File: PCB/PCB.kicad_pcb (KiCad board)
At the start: 2 copper layers, 50 parts, among them J2 Conn_01x02_Pin, J3 Conn_01x02_Pin, J5 Conn_01x04_Pin, SW1 SW_Push, U1 STM32L476RGTx, U2 FGPMMOPA6H, U4 TPS63001DRCR, U5 LM2735XMF/NOPB, U8 LM386, U9 MAX7375AXR805

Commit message: Add files via upload
Finished PCB, awaiting check from professor and TAs
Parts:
- added H1: MountingHole, MountingHole:MountingHole_2.1mm, F.Cu at (232.4, 141.0)
- added H2: MountingHole, MountingHole:MountingHole_2.1mm, F.Cu at (209.6, 88.9)
- added H3: MountingHole, MountingHole:MountingHole_2.1mm, F.Cu at (184.2, 116.8)
- added H4: MountingHole, MountingHole:MountingHole_2.1mm, F.Cu at (185.4, 139.7)
- moved U3 111.5 mm to (200.7, 135.9), turned to -90 degrees
- moved C11 90.8 mm to (185.4, 124.6), turned to 90 degrees
- moved C1 90.5 mm to (206.2, 97.2)
- moved C2 90.5 mm to (206.2, 104.2)
- moved C3 90.5 mm to (178.2, 106.0)
- moved C4 90.5 mm to (183.2, 96.5)
- moved C5 90.5 mm to (192.7, 105.1)
- moved D1 90.5 mm to (196.7, 97.6)
- moved D3 90.5 mm to (193.2, 95.9)
- moved J2 90.5 mm to (199.2, 88.5)
- moved L1 90.5 mm to (210.7, 100.7)
- moved L2 90.5 mm to (181.0, 91.0)
- moved R1 90.5 mm to (183.2, 104.0)
- moved R2 90.5 mm to (187.7, 96.5)
- moved R3 90.5 mm to (183.3, 99.5)
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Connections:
- U1 pad 24: unconnected-(U1-PC4-Pad24) -> /LoRa RX
- U1 pad 25: unconnected-(U1-PC5-Pad25) -> /LoRa TX
- U1 pad 27: /Debug 4 -> unconnected-(U1-PB1-Pad27)
- U1 pad 28: /Debug 3 -> unconnected-(U1-PB2-Pad28)
- U1 pad 29: /Debug 2 -> unconnected-(U1-PB10-Pad29)
- U1 pad 30: /Debug 1 -> unconnected-(U1-PB11-Pad30)
- U1 pad 33: unconnected-(U1-PB12-Pad33) -> /Debug 4
- U1 pad 34: unconnected-(U1-PB13-Pad34) -> /Debug 2
- U1 pad 35: unconnected-(U1-PB14-Pad35) -> /Debug 3
- U1 pad 36: unconnected-(U1-PB15-Pad36) -> /Debug 1
- U1 pad 53: /LoRa RX -> unconnected-(U1-PC12-Pad53)
- U1 pad 54: /LoRa TX -> unconnected-(U1-PD2-Pad54)
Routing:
- net GND: track 105.9 -> 231.3 mm, vias 21 -> 59
- net +3.3V: track 67.0 -> 145.3 mm, vias 5 -> 9
- net /RST: track 19.1 -> 63.4 mm
- net /GPS RX: track 0.00 -> 35.3 mm, vias 0 -> 2
- net /GPS TX: track 0.00 -> 31.3 mm, vias 0 -> 2
- net +5V: track 28.2 -> 58.1 mm, vias 3 -> 5
- net /SWCLK: track 0.00 -> 28.9 mm, vias 0 -> 1
- net /SWDIO: track 0.00 -> 23.9 mm, vias 0 -> 1
- net /LoRa TX: track 0.00 -> 20.5 mm, vias 0 -> 1
- net /LoRa RX: track 0.00 -> 17.7 mm, vias 0 -> 1
- net /Debug 3: track 0.00 -> 17.3 mm
- net /DAC OUT: track 0.00 -> 16.7 mm, vias 0 -> 1
- net /Debug 2: track 0.00 -> 16.3 mm
- net /Debug 1: track 0.00 -> 15.2 mm
- net /Debug 4: track 0.00 -> 11.5 mm
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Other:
- board text added: "ECE 477 Team 5: Smart Dog Collar Andrew Wu Nick Durnil David Manojlovic Ethan James Version 2"

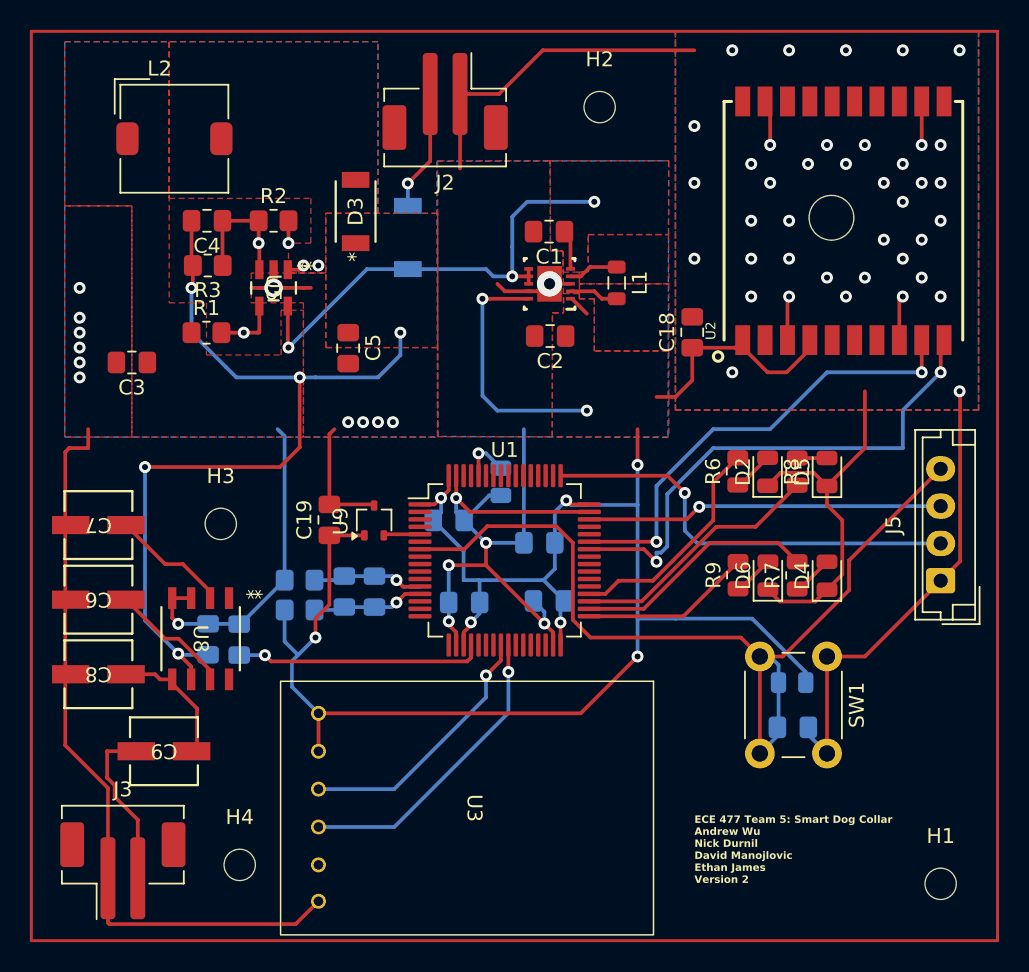
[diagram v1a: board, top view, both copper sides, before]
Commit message: Exlusion Zones added
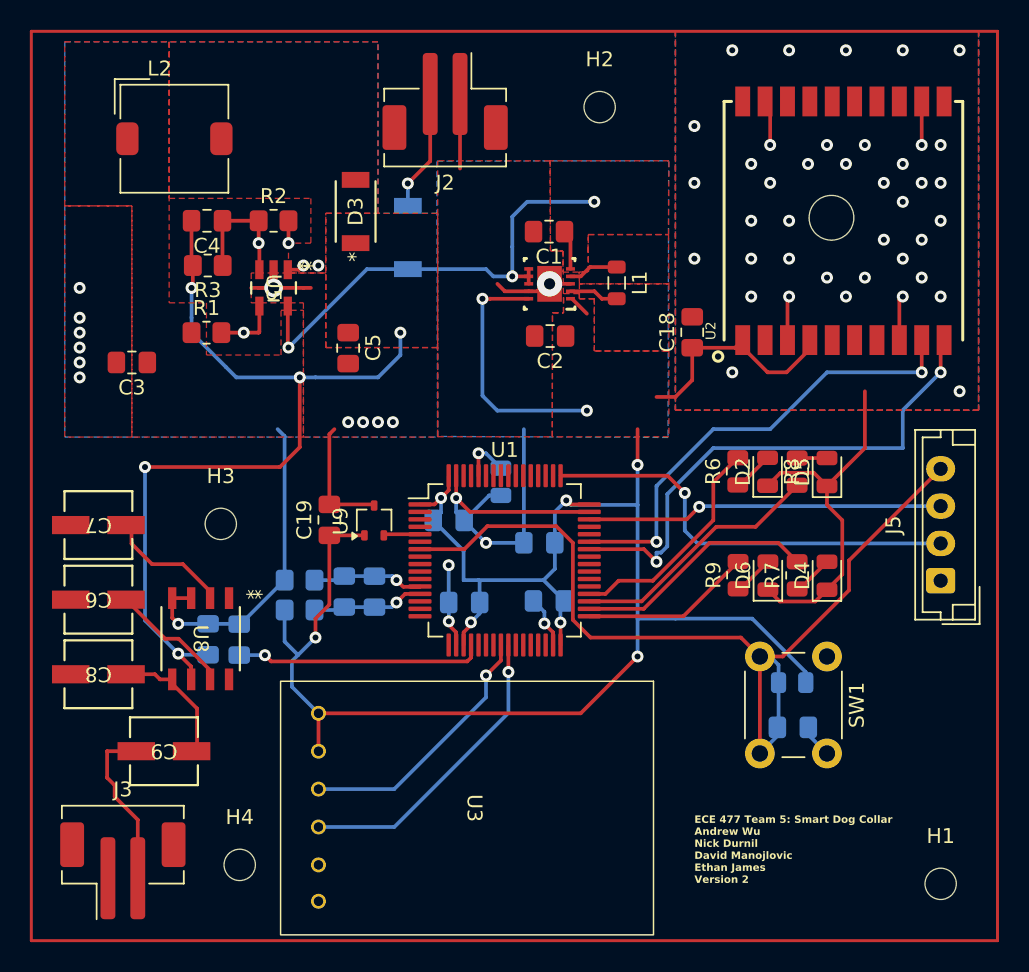
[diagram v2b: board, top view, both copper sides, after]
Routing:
- net GND: track 231.3 -> 124.1 mm
- net /- Amp: track 7.93 -> 8.44 mm

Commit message: DRC Error fixes
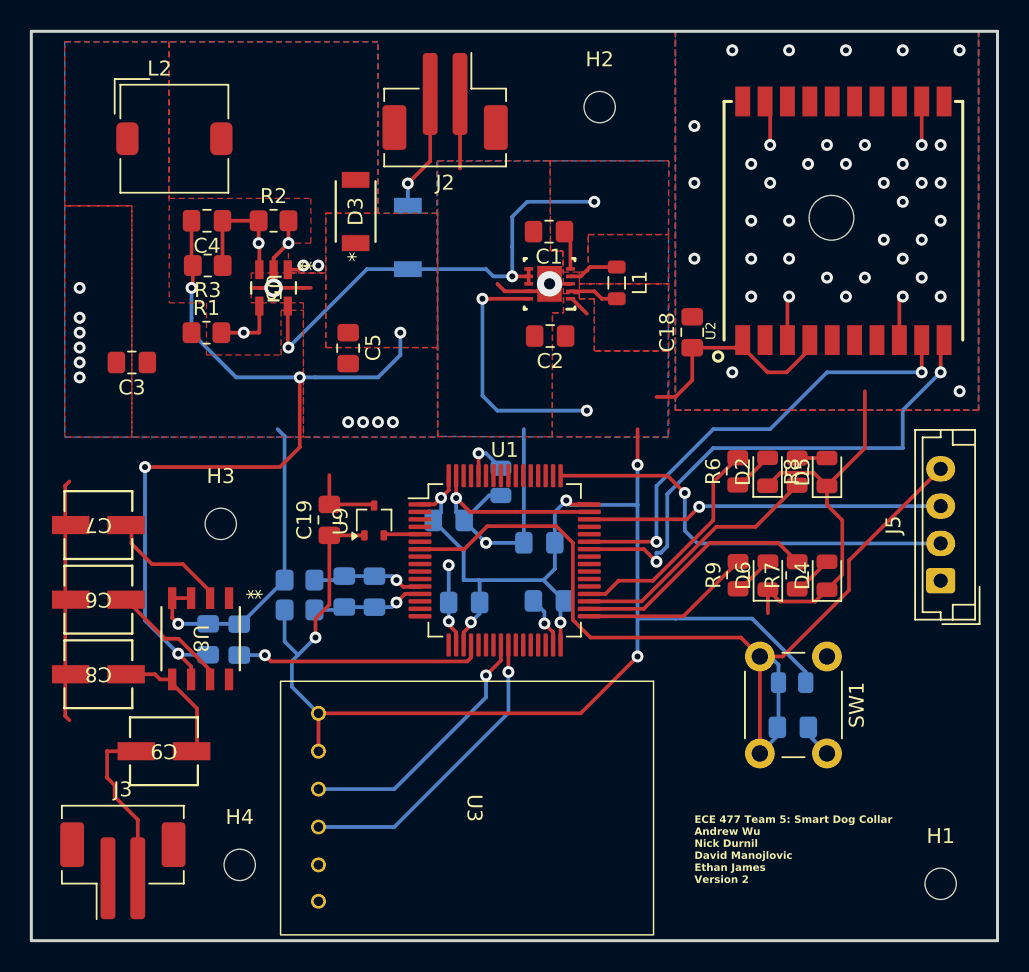
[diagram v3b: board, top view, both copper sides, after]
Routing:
- net GND: track 124.1 -> 141.8 mm
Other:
- board outline added: 64.8 x 61 mm
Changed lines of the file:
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@@
 		)
 		(fill none)
-		(layer "F.Cu")
-		(net 2)
+		(layer "Edge.Cuts")
 	)
 	(gr_text "ECE 477 Team 5: Smart Dog Collar\nAndrew Wu\nNick Durnil\nDavid Manojlovic\nEthan James\nVersion 2"
@@
 	)
 	(segment
-		(start 191.43 115.535)
-		(end 191.43 110.83)
-		(width 0.25)
-		(layer "F.Cu")
-		(net 2)
-	)
-	(segment
 		(start 222.14 104.52)
 		(end 222.14 101.71)
@@
 	)
 	(segment
+		(start 173.7253 129.7253)
+		(end 174 130)
+		(width 0.25)
+		(layer "F.Cu")
+		(net 2)
+	)
+	(segment
 		(start 220.82801 121.243481)
 		(end 221.627029 122.0425)
@@
 	)
 	(segment
+		(start 173.7253 114.2747)
+		(end 174 114)
+		(width 0.25)
+		(layer "F.Cu")
+		(net 2)
+	)
+	(segment
 		(start 205.362145 101.247732)
 		(end 204.792148 101.247732)
@@
 	)
 	(segment
-		(start 187.69 99.8008)
-		(end 187.69 101.02)
+		(start 220.82801 121.243481)
+		(end 220.82801 122.82801)
+		(width 0.25)
+		(layer "F.Cu")
+		(net 2)
+	)
+	(segment
+		(start 173.7253 116.5537)
+		(end 173.7253 114.2747)
+		(width 0.25)
+		(layer "F.Cu")
+		(net 2)
+	)
+	(segment
+		(start 174.0916 126.92)
+		(end 173.7253 127.2863)
 		(width 0.25)
 		(layer "F.Cu")
@@
 	)
 	(segment
+		(start 173.7253 127.2863)
+		(end 173.7253 129.7253)
+		(width 0.25)
+		(layer "F.Cu")
+		(net 2)
+	)
+	(segment
 		(start 182.165 121.81585)
 		(end 180.895 121.81585)
@@
 	)
 	(segment
+		(start 174.0916 116.92)
+		(end 173.7253 116.5537)
+		(width 0.25)
+		(layer "F.Cu")
+		(net 2)
+	)
+	(segment
+		(start 187.69 99.02)
+		(end 188.69 98.02)
+		(width 0.25)
+		(layer "F.Cu")
+		(net 2)
+	)
+	(segment
 		(start 186.69 101.02)
 		(end 187.69 101.02)
@@
 	)
 	(segment
+		(start 191.43 115.535)
+		(end 191.43 113.57)
+		(width 0.25)
+		(layer "F.Cu")
+		(net 2)
+	)
+	(segment
+		(start 173.7253 126.5537)
+		(end 173.7253 122.2863)
+		(width 0.25)
+		(layer "F.Cu")
+		(net 2)
+	)
+	(segment
 		(start 221.675735 113.4125)
 		(end 223.9025 113.4125)
@@
 	)
 	(segment
+		(start 187.69 99.8008)
+		(end 187.69 99.02)
+		(width 0.25)
+		(layer "F.Cu")
+		(net 2)
+	)
+	(segment
 		(start 180.895 121.81585)
 		(end 180.895 123.135)
@@
 	)
 	(segment
+		(start 174.0916 126.92)
+		(end 173.7253 126.5537)
+		(width 0.25)
+		(layer "F.Cu")
+		(net 2)
+	)
+	(segment
 		(start 220.98 89.36)
 		(end 220.98 91.44)
@@
 	)
 	(segment
+		(start 173.7253 121.5537)
+		(end 173.7253 117.2863)
+		(width 0.25)
+		(layer "F.Cu")
+		(net 2)
+	)
+	(segment
 		(start 186.69 101.02)
 		(end 186.19 101.02)
@@
 	)
 	(segment
+		(start 187.69 99.8008)
+		(end 187.69 101.02)
+		(width 0.25)
+		(layer "F.Cu")
+		(net 2)
+	)
+	(segment
 		(start 221.627029 122.0425)
 		(end 224.0025 122.0425)
@@
 	)
 	(segment
+		(start 173.7253 122.2863)
+		(end 174.0916 121.92)
+		(width 0.25)
+		(layer "F.Cu")
+		(net 2)
+	)
+	(segment
+		(start 173.7253 117.2863)
+		(end 174.0916 116.92)
+		(width 0.25)
+		(layer "F.Cu")
+		(net 2)
+	)
+	(segment
 		(start 204.792148 101.247732)
 		(end 203.19215 101.247732)
@@
 	)
 	(segment
-		(start 191.43 110.83)
-		(end 191.77 110.49)
+		(start 174.0916 121.92)
+		(end 173.7253 121.5537)
 		(width 0.25)
 		(layer "F.Cu")
@@
 		(polygon
 			(pts
-				(xy 190.5 114) (xy 190.5 119) (xy 196 119) (xy 196 114)
+				(xy 190 114) (xy 190 119) (xy 196 119) (xy 196 114)
 			)
 		)
@@
 		(net_name "")
 		(layers "F&B.Cu")
-		(name "Mounting Hole")
 		(hatch edge 0.5)
 		(connect_pads
@@
 		(polygon
 			(pts
-				(xy 181.5 114.5) (xy 181.5 119) (xy 187 119) (xy 187 114.5)
+				(xy 181.5 114) (xy 187 114) (xy 187 119) (xy 186 119) (xy 184 119.5) (xy 182.5 119) (xy 181.5 119)
 			)
 		)
@@
 		(polygon
 			(pts
-				(xy 207 86.5) (xy 207 91.5) (xy 212.5 91.5) (xy 212.5 86.5)
+				(xy 206.815912 86.399459) (xy 206.815912 91.399459) (xy 212.315912 91.399459) (xy 212.315912 86.399459)
 			)
 		)

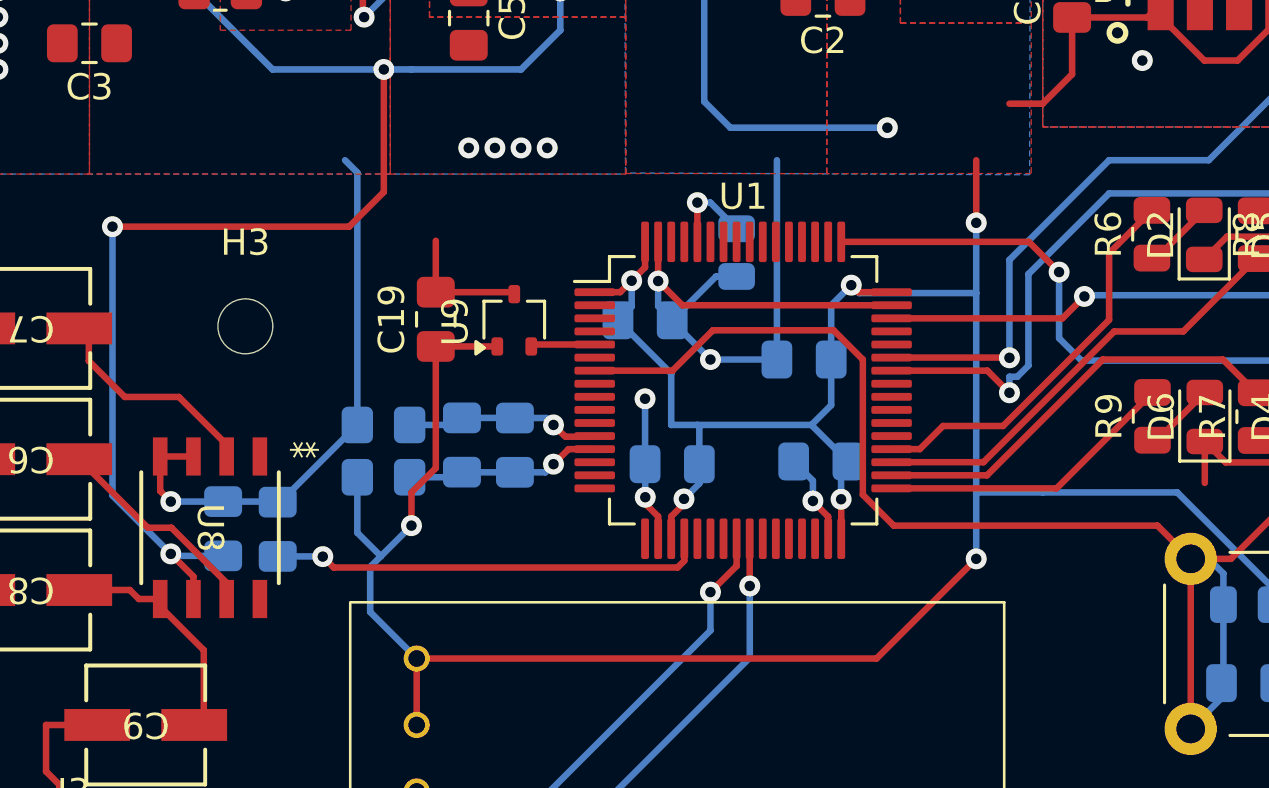
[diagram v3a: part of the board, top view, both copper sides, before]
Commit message: Debug vias added
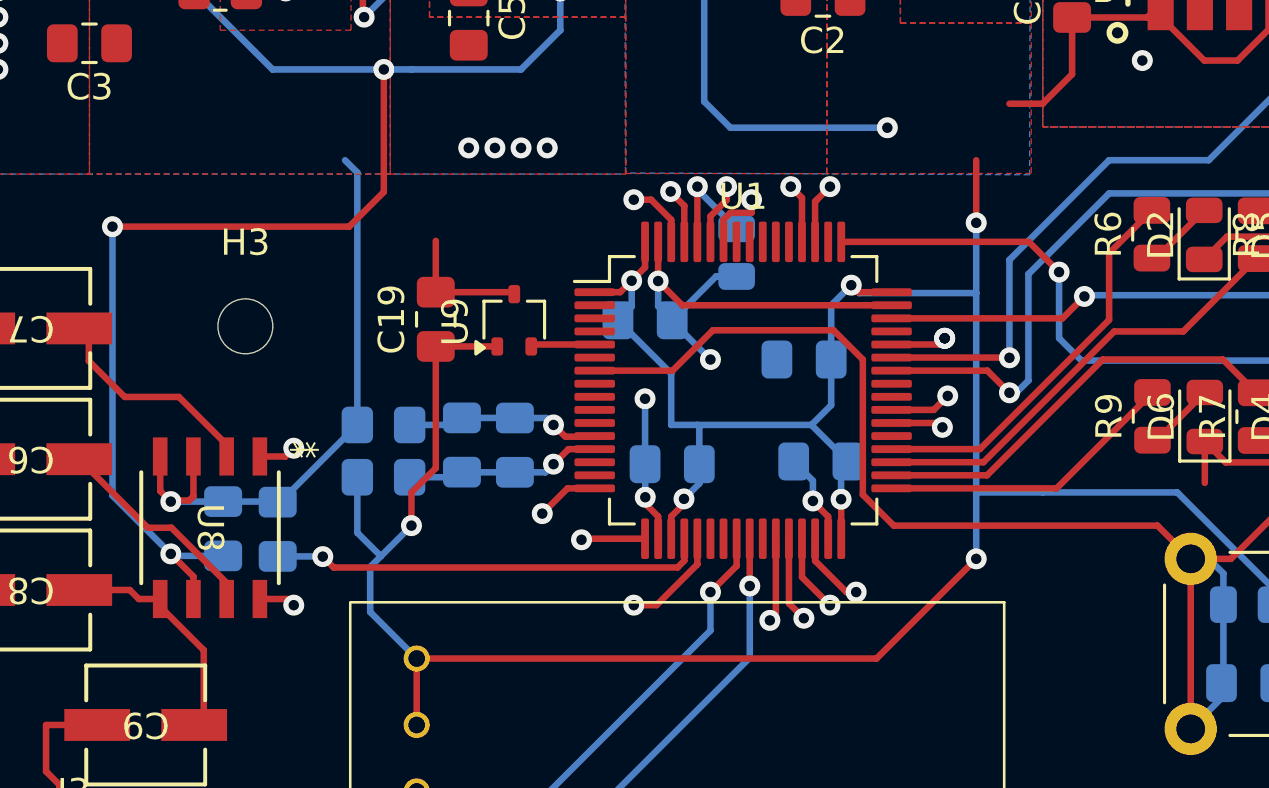
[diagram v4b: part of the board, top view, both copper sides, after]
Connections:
- U1 pad 16: unconnected-(U1-PA2-Pad16) -> /USART 2 TX
- U1 pad 17: unconnected-(U1-PA3-Pad17) -> /USART 2 RX
- U1 pad 21: unconnected-(U1-PA5-Pad21) -> /DAC 2
- U1 pad 27: unconnected-(U1-PB1-Pad27) -> /PB1
- U1 pad 28: unconnected-(U1-PB2-Pad28) -> /PB2
- U1 pad 29: unconnected-(U1-PB10-Pad29) -> /USART 3 TX
- U1 pad 30: unconnected-(U1-PB11-Pad30) -> /USART 3 RX
- U1 pad 38: unconnected-(U1-PC7-Pad38) -> /PC7
- U1 pad 39: unconnected-(U1-PC8-Pad39) -> /PC8
- U1 pad 44: unconnected-(U1-PA11-Pad44) -> /PA 11
- U1 pad 51: unconnected-(U1-PC10-Pad51) -> /UART TX
- U1 pad 52: unconnected-(U1-PC11-Pad52) -> /UART RX
- U1 pad 58: unconnected-(U1-PB6-Pad58) -> /TIM 4 CH 1
- U1 pad 59: unconnected-(U1-PB7-Pad59) -> /TIM 4 CH 2
- U1 pad 61: unconnected-(U1-PB8-Pad61) -> /TIM 4 CH 3
- U1 pad 62: unconnected-(U1-PB9-Pad62) -> /TIM 4 CH 4
- U8 pad 1: unconnected-(U8-GAIN-Pad1) -> /Gain 1
- U8 pad 8: unconnected-(U8-GAIN-Pad8) -> /Gain 2
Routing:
- net GND: track 141.8 -> 132.9 mm
- net /DAC 2: track 0.00 -> 4.06 mm, vias 0 -> 1
- net /PB2: track 0.00 -> 3.28 mm, vias 0 -> 1
- net /PB1: track 0.00 -> 3.22 mm, vias 0 -> 1
- net /USART 3 TX: track 0.00 -> 2.98 mm, vias 0 -> 1
- net /USART 3 RX: track 0.00 -> 2.91 mm, vias 0 -> 1
- net /TIM 4 CH 4: track 0.00 -> 2.59 mm, vias 0 -> 1
- net /TIM 4 CH 1: track 0.00 -> 2.52 mm, vias 0 -> 1
- net /USART 2 RX: track 0.00 -> 2.45 mm, vias 0 -> 1
- net /USART 2 TX: track 0.00 -> 2.40 mm, vias 0 -> 1
- net /PC8: track 0.00 -> 2.37 mm, vias 0 -> 1
- net /TIM 4 CH 2: track 0.00 -> 2.37 mm, vias 0 -> 1
- net /UART TX: track 0.00 -> 2.35 mm, vias 0 -> 1
- net /UART RX: track 0.00 -> 2.29 mm, vias 0 -> 1
- net /TIM 4 CH 3: track 0.00 -> 2.27 mm, vias 0 -> 1
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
